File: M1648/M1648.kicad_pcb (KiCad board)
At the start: 2 copper layers, 99.9 x 64.5 mm, 15 parts, among them J1 Z50Bus, U1 74LS86, U2 74LS04, U3 74LS139, U4 28C256, U5 CY62256-70PC, U6 CY62256-70PC

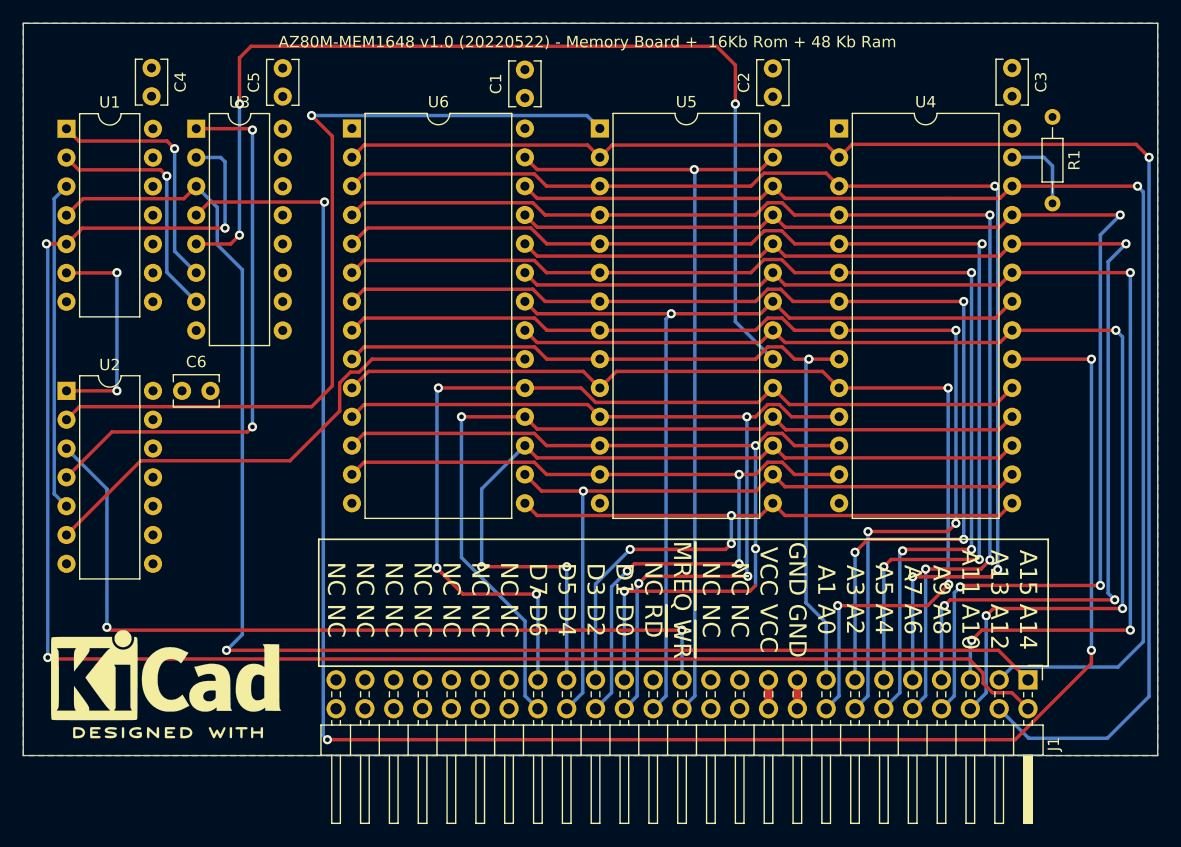
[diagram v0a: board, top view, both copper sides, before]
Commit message: Fix: il segnale A14' adesso è applicato a U6
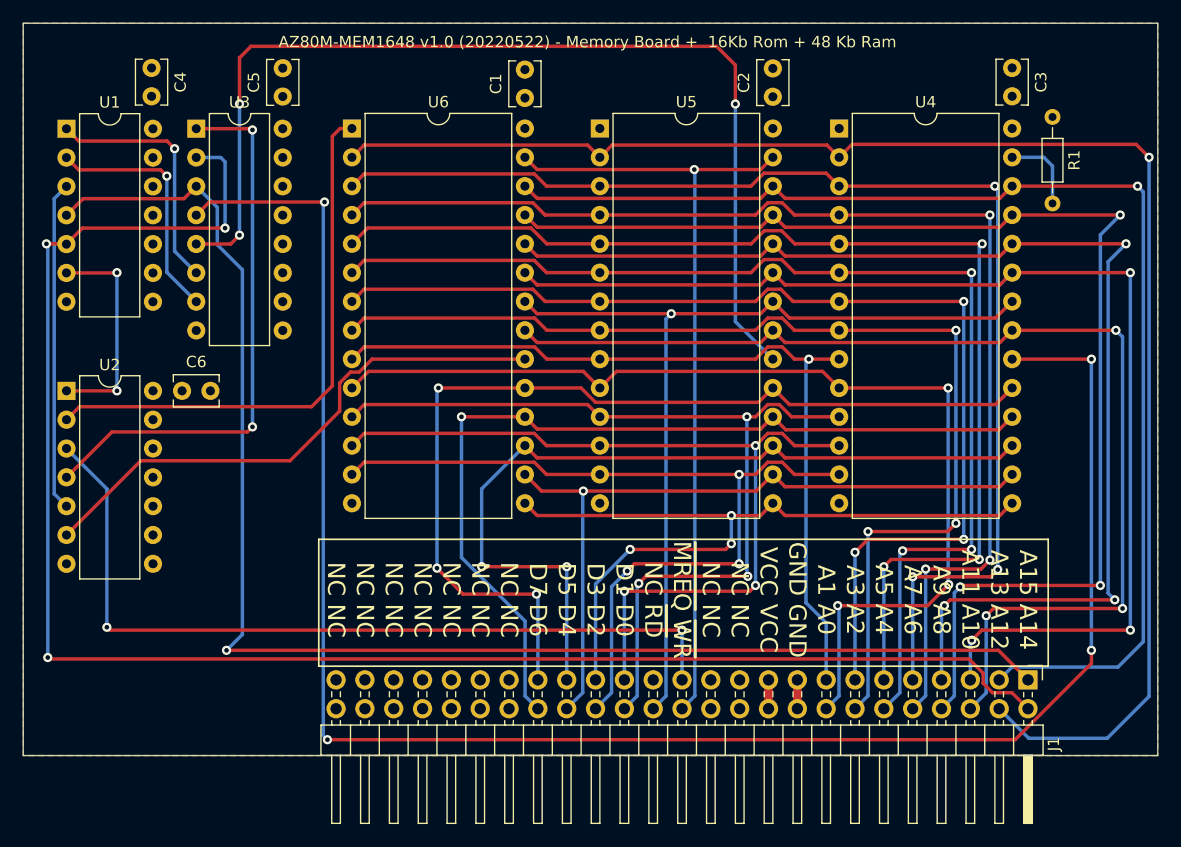
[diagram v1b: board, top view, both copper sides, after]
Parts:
- removed REF**: KiCad-Logo2_8mm_SilkScreen, Symbol:KiCad-Logo2_8mm_SilkScreen
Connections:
- U5 pad 1: A14' -> GND
- U6 pad 1: GND -> A14'
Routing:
- net A14': track 75.1 -> 48.7 mm, vias 1 -> 0
